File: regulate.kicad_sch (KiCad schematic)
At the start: 15 parts, among them J9 Conn_01x04_Pin, U2 LTC2990

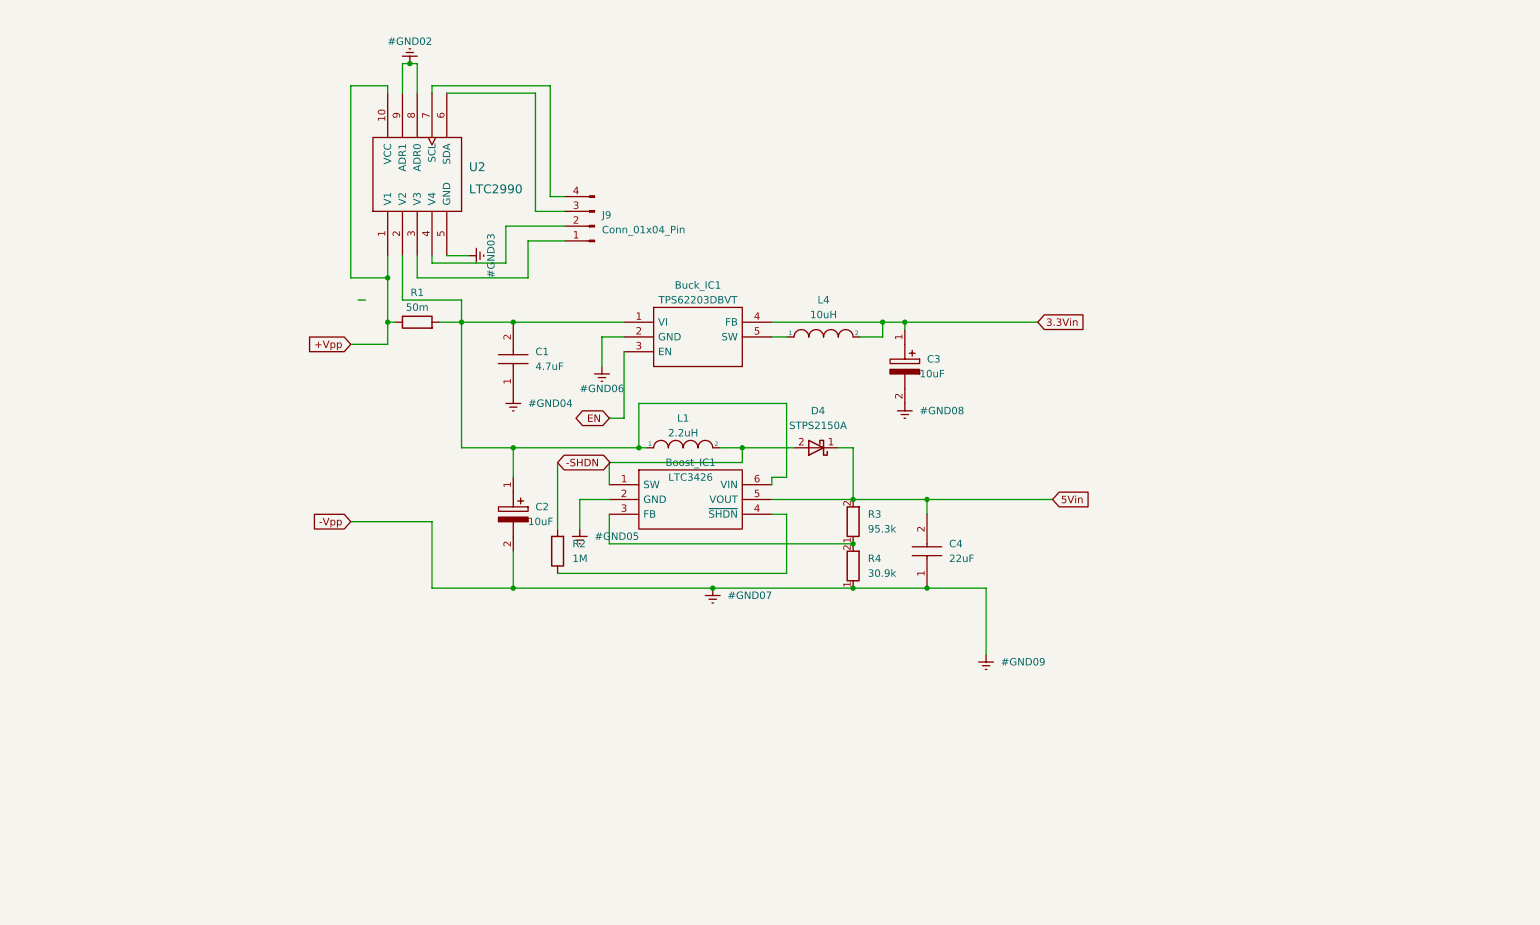
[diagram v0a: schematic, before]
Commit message: Final Schematic
Final Schematic. PC104 pins not assigned.
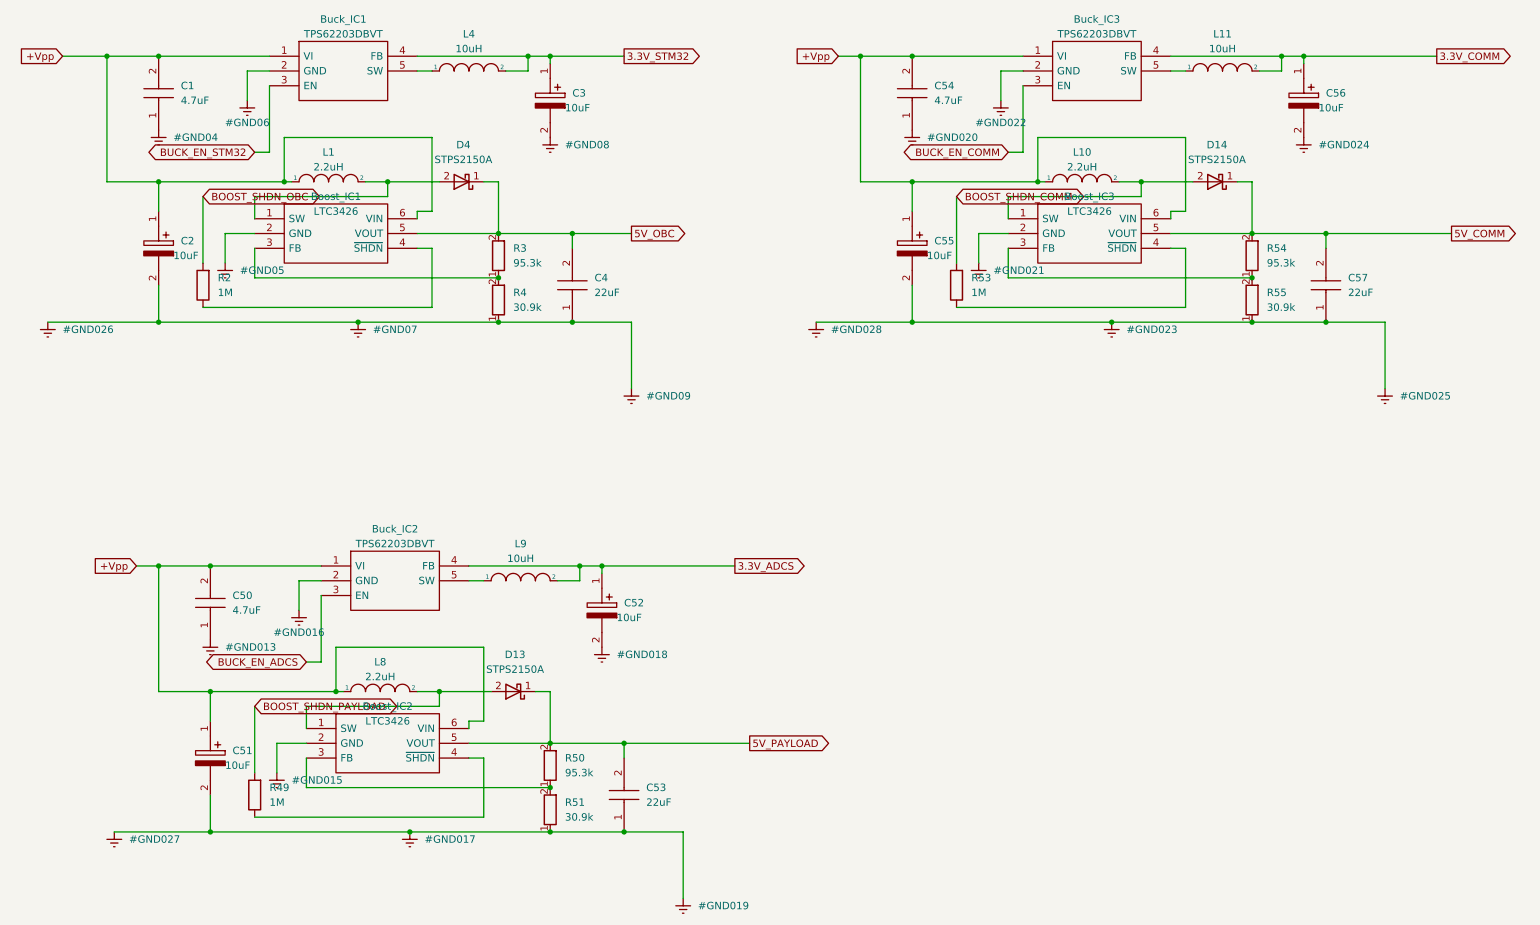
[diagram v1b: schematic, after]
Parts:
- removed J9: Conn_01x04_Pin, Connector_PinHeader_2.54mm:PinHeader_1x04_P2.54mm_Vertical, symbol Connector:Conn_01x04_Pin
- removed R1: 50m, 50m RST:RESC3216X88N, symbol Device:R
- removed U2: LTC2990, MON & PROTECC:SOP50P490X110-10N, symbol curr volt mon:LTC2990
- added Boost_IC2, Boost_IC3: LTC3426, Boost LTC3426:SOT95P280X90-6N, symbol boost sat:LTC3426ES6#TRMPBF
- added Buck_IC2, Buck_IC3: TPS62203DBVT, BUck TPS62203DBVT:SOT95P280X145-5N, symbol bucki c1:TPS62203DBVT
- added C50, C54: 4.7uF, cap 4.7uf:C1210, symbol Cap 4.7uf:C1210C475K4RACAUTO
- added C51, C52, C55, C56: 10uF, 10uF MLCC:CAPC2012X94N, symbol EXTRAs:AFK106M35C12T-F
- added C53, C57: 22uF, cap 22uF low esr and esl:C3216_Commercial, symbol cap22uf:ZRB18AR61A226ME01L
- added D13, D14: STPS2150A, Schottky DD with stock:DIOM5126X265N, symbol Device:D_Schottky
- added L10, L8: 2.2uH, indc 2.2uH:IHLP2020CZER2R2M8A, symbol pspice:INDUCTOR
- added L11, L9: 10uH, indc 10uH crct:SRN1060-100M, symbol pspice:INDUCTOR
- added R49, R53: 1M, 1MEGA RST:RESC1608X55N, symbol Device:R
- added R50, R54: 95.3k, rst 95.3k:RESC2012X60N, symbol Device:R
- added R51, R55: 30.9k, rst 30.9k:RC0603FR-0730K9L, symbol Device:R
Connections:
- net +Vpp: now also Boost_IC1.6 (VIN), Buck_IC1.1 (VI), C1.2, C2.1, L1.1, Boost_IC2.6 (VIN), Boost_IC3.6 (VIN), Buck_IC2.1 (VI), Buck_IC3.1 (VI), C50.2, C51.1, C54.2, C55.1, L10.1, L8.1
- net Earth: now also Boost_IC2.2 (GND), Boost_IC3.2 (GND), Buck_IC2.2 (GND), Buck_IC3.2 (GND), C50.1, C51.2, C52.2, C53.1, C54.1, C55.2, C56.2, C57.1, R51.1, R55.1
- net -SHDN renamed BOOST_SHDN_OBC
- net 3.3Vin renamed 3.3V_STM32
- net 5Vin renamed 5V_OBC
- net EN renamed BUCK_EN_STM32
- new net: Buck_IC2.5 (SW), L9.1
- new net: Boost_IC2.1 (SW), D13.2 (A), L8.2
- new net: Boost_IC2.3 (FB), R50.1, R51.2
- new net: Buck_IC3.5 (SW), L11.1
- new net: Boost_IC3.1 (SW), D14.2 (A), L10.2
- new net: Boost_IC3.3 (FB), R54.1, R55.2
- new net: Boost_IC3.4 (~{SHDN}), R53.1
- new net: Boost_IC2.4 (~{SHDN}), R49.1
- new net 3.3V_ADCS: Buck_IC2.4 (FB), C52.1, L9.2
- new net 3.3V_COMM: Buck_IC3.4 (FB), C56.1, L11.2
- new net 5V_COMM: Boost_IC3.5 (VOUT), C57.2, D14.1 (K), R54.2
- new net 5V_PAYLOAD: Boost_IC2.5 (VOUT), C53.2, D13.1 (K), R50.2
- new net BOOST_SHDN_COMM: R53.2
- new net BOOST_SHDN_PAYLOAD: R49.2
- new net BUCK_EN_ADCS: Buck_IC2.3 (EN)
- new net BUCK_EN_COMM: Buck_IC3.3 (EN)

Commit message: Ready to rearrange
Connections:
- net 3.3V_STM32 renamed +3.3V
- net 5V_OBC renamed 5V
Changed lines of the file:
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@@
     )
   )
-  (global_label "5V_OBC" (shape output) (at 127 71.12 0) (fields_autoplaced)
+  (global_label "5V" (shape output) (at 127 71.12 0) (fields_autoplaced)
     (effects (font (size 1.27 1.27)) (justify left))
-    (property "Intersheetrefs" "${INTERSHEET_REFS}" (at 137.042 71.12 0)
+    (property "Intersheetrefs" "${INTERSHEET_REFS}" (at 132.2039 71.12 0)
       (effects (font (size 1.27 1.27)) (justify left) hide)
     )
@@
     )
   )
-  (global_label "3.3V_STM32" (shape output) (at 125.73 40.64 0) (fields_autoplaced)
+  (global_label "+3.3V" (shape output) (at 125.73 40.64 0) (fields_autoplaced)
     (effects (font (size 1.27 1.27)) (justify left))
-    (property "Intersheetrefs" "${INTERSHEET_REFS}" (at 139.7633 40.64 0)
+    (property "Intersheetrefs" "${INTERSHEET_REFS}" (at 134.3206 40.64 0)
       (effects (font (size 1.27 1.27)) (justify left) hide)
     )

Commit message: LIBS + 3D EXPORT, Ready to reroute
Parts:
- L1, L10, L8: footprint indc 2.2uH:IHLP2020CZER2R2M8A -> 1uH indc:IHHP0805ZHER1R0M01
- L11, L4, L9: footprint indc 10uH crct:SRN1060-100M -> indc 2.2uH:IHLP2020CZER2R2M8A
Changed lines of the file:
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@@
       (effects (font (size 1.27 1.27)))
     )
-    (property "Footprint" "indc 2.2uH:IHLP2020CZER2R2M8A" (at 83.82 149.86 0)
+    (property "Footprint" "1uH indc:IHHP0805ZHER1R0M01" (at 83.82 149.86 0)
       (effects (font (size 1.27 1.27)) hide)
     )
@@
       (effects (font (size 1.27 1.27)))
     )
-    (property "Footprint" "indc 10uH crct:SRN1060-100M" (at 228.6 43.18 0)
+    (property "Footprint" "indc 2.2uH:IHLP2020CZER2R2M8A" (at 228.6 43.18 0)
       (effects (font (size 1.27 1.27)) hide)
     )
@@
       (effects (font (size 1.27 1.27)))
     )
-    (property "Footprint" "indc 10uH crct:SRN1060-100M" (at 107.95 130.81 0)
+    (property "Footprint" "indc 2.2uH:IHLP2020CZER2R2M8A" (at 107.95 130.81 0)
       (effects (font (size 1.27 1.27)) hide)
     )
@@
       (effects (font (size 1.27 1.27)))
     )
-    (property "Footprint" "indc 2.2uH:IHLP2020CZER2R2M8A" (at 74.93 62.23 0)
+    (property "Footprint" "1uH indc:IHHP0805ZHER1R0M01" (at 74.93 62.23 0)
       (effects (font (size 1.27 1.27)) hide)
     )
@@
       (effects (font (size 1.27 1.27)))
     )
-    (property "Footprint" "indc 2.2uH:IHLP2020CZER2R2M8A" (at 204.47 62.23 0)
+    (property "Footprint" "1uH indc:IHHP0805ZHER1R0M01" (at 204.47 62.23 0)
       (effects (font (size 1.27 1.27)) hide)
     )
@@
       (effects (font (size 1.27 1.27)))
     )
-    (property "Footprint" "indc 10uH crct:SRN1060-100M" (at 99.06 43.18 0)
-      (effects (font (size 1.27 1.27)) hide)
-    )
+    (property "Footprint" "indc 2.2uH:IHLP2020CZER2R2M8A" (at 99.06 43.18 0)
+      (effects (font (size 1.27 1.27)) hide)
+    )

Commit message: updates
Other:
- moved on the sheet: Boost_IC2, Boost_IC3, Buck_IC2, Buck_IC3, C50, C51, C52, C53, C54, C55, C56, C57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
